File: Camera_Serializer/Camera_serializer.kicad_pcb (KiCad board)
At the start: 4 copper layers, 38.1 x 38.1 mm, 87 parts, among them J2 F32Q-1A7H1-11022, Q1 BSS138, Q2 BSS138, U2 PUSB3FR4Z, U3 TPS62133RGTR, U4 TPS62131RGTT, U5 TPS73601DBVR, U6 MIC5528-3.3YMT-TR

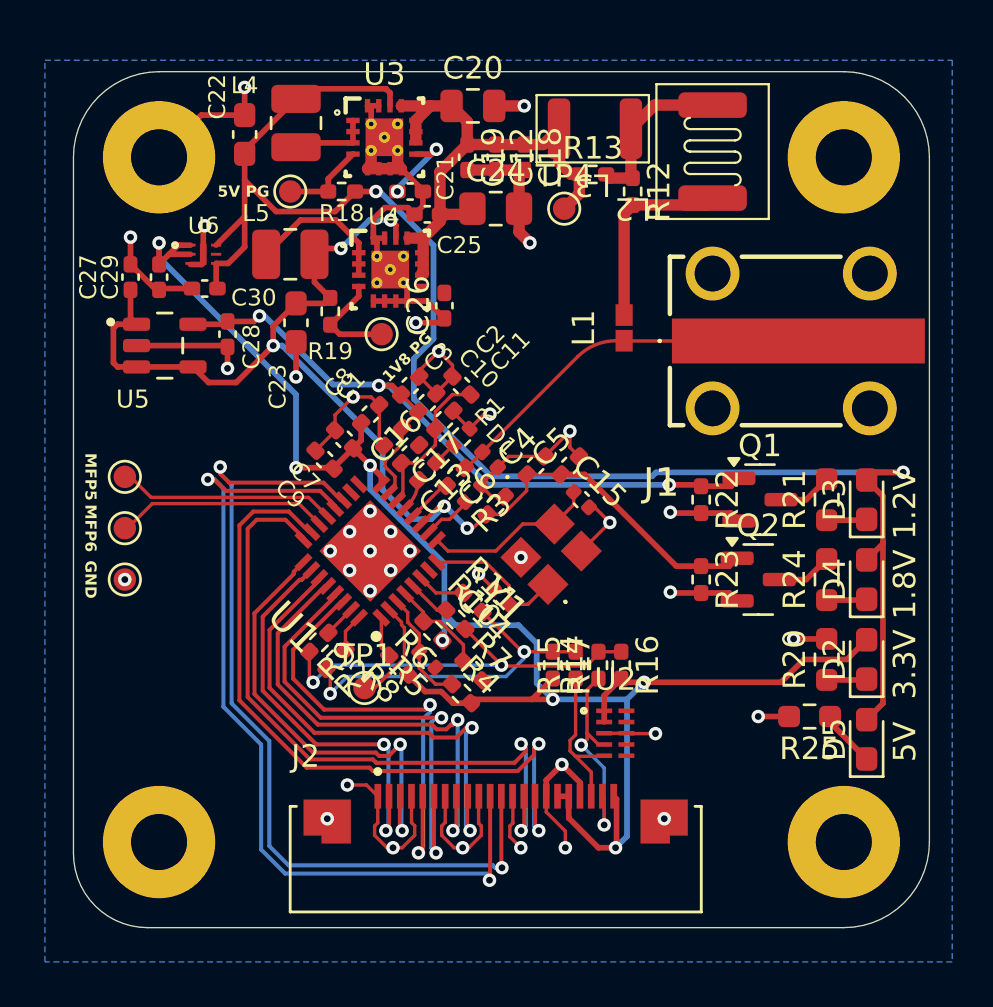
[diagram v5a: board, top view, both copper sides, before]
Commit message: Finished differential routing
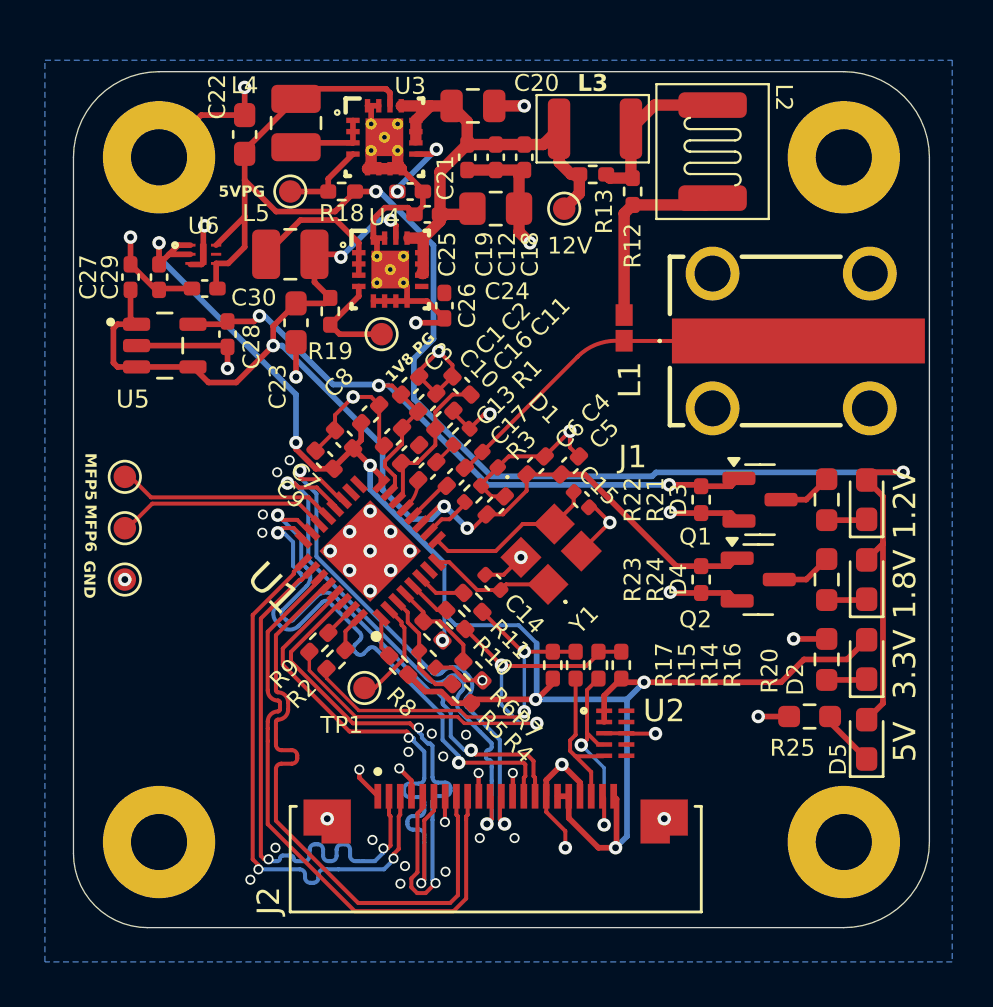
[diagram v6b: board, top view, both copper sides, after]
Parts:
- removed 1V8 PG: TestPoint, TestPoint:TestPoint_Pad_D1.0mm
- removed 5V PG: TestPoint, TestPoint:TestPoint_Pad_D1.0mm
- removed GND, MFP5, MFP6: TestPoint, TestPoint:TestPoint_Pad_D1.0mm
- added TP2: TestPoint, TestPoint:TestPoint_Pad_D1.0mm, F.Cu at (134.4, 94.7)
- added TP3: TestPoint, TestPoint:TestPoint_Pad_D1.0mm, F.Cu at (134.4, 97.0)
- added TP5: TestPoint, TestPoint:TestPoint_Pad_D1.0mm, F.Cu at (141.7, 82.0)
- added TP7: TestPoint, TestPoint:TestPoint_Pad_D1.0mm, F.Cu at (145.8, 88.4)
- added TP8: TestPoint, TestPoint:TestPoint_Pad_D1.0mm, F.Cu at (134.4, 99.3)
- moved C14 0.74 mm to (150.7, 99.4)
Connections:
- C26 pad 2: Net-(U4-SS_TR) -> unconnected-(C26-Pad2)
- L5 pad 1: Net-(L5-Pad1) -> unconnected-(L5-Pad1)
- R19 pad 2: Net-(U4-PG) -> Net-(R19-Pad2)
- U4 pad 1: Net-(L5-Pad1) -> unconnected-(U4-SW-Pad1)
- U4 pad 10: +12V -> unconnected-(U4-AVIN-Pad10)
- U4 pad 11: +12V -> unconnected-(U4-PVIN-Pad11)
- U4 pad 12: +12V -> unconnected-(U4-PVIN-Pad12)
- U4 pad 13: +12V -> unconnected-(U4-EN-Pad13)
- U4 pad 14: +1V8 -> unconnected-(U4-VOS-Pad14)
- U4 pad 15: GND -> unconnected-(U4-PGND-Pad15)
- U4 pad 16: GND -> unconnected-(U4-PGND-Pad16)
- U4 pad 17: GND -> unconnected-(U4-EP-Pad17)
- U4 pad 18: (no net) -> GND
- U4 pad 19: (no net) -> GND
- U4 pad 2: Net-(L5-Pad1) -> unconnected-(U4-SW-Pad2)
- U4 pad 20: (no net) -> GND
- U4 pad 21: (no net) -> GND
- U4 pad 3: Net-(L5-Pad1) -> unconnected-(U4-SW-Pad3)
- U4 pad 4: Net-(U4-PG) -> unconnected-(U4-PG-Pad4)
- U4 pad 5: GND -> unconnected-(U4-FB-Pad5)
- U4 pad 6: GND -> unconnected-(U4-AGND-Pad6)
- U4 pad 7: GND -> unconnected-(U4-FSW-Pad7)
- U4 pad 8: GND -> unconnected-(U4-DEF-Pad8)
- U4 pad 9: Net-(U4-SS_TR) -> unconnected-(U4-SS_TR-Pad9)
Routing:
- net /csi/CSI.D2_N: track 38.5 -> 24.6 mm
- net /csi/CSI.D2_P: track 38.0 -> 24.6 mm
- net /csi/CSI.D3_P: track 32.5 -> 24.6 mm
- net /csi/CSI.CK_N: track 21.0 -> 27.7 mm, vias 2 -> 0
- net Net-(L5-Pad1): track 6.61 -> 0.00 mm
- net (no net): track 0.00 -> 6.61 mm, vias 0 -> 2
- net GND: track 102.3 -> 96.1 mm, vias 38 -> 53
- net /csi/CSI.D0_N: track 18.5 -> 24.6 mm
- net /csi/CSI.D3_N: track 30.4 -> 24.6 mm
- net /csi/I2C.SDA: track 18.1 -> 23.6 mm
- net /csi/CSI.CK_P: track 22.3 -> 27.7 mm, vias 2 -> 0
- net /csi/CSI.D0_P: track 20.1 -> 24.6 mm
- net /csi/CSI.D1_N: track 20.6 -> 24.7 mm
- net /csi/CSI.D1_P: track 21.5 -> 24.6 mm
- net /csi/I2C.SCL: track 15.6 -> 17.6 mm
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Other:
- board text added: "12V"
- board text added: "1V8 PG"
- board text added: "5VPG"
- board text added: "GND"
- board text added: "MFP5"
- board text added: "MFP6"

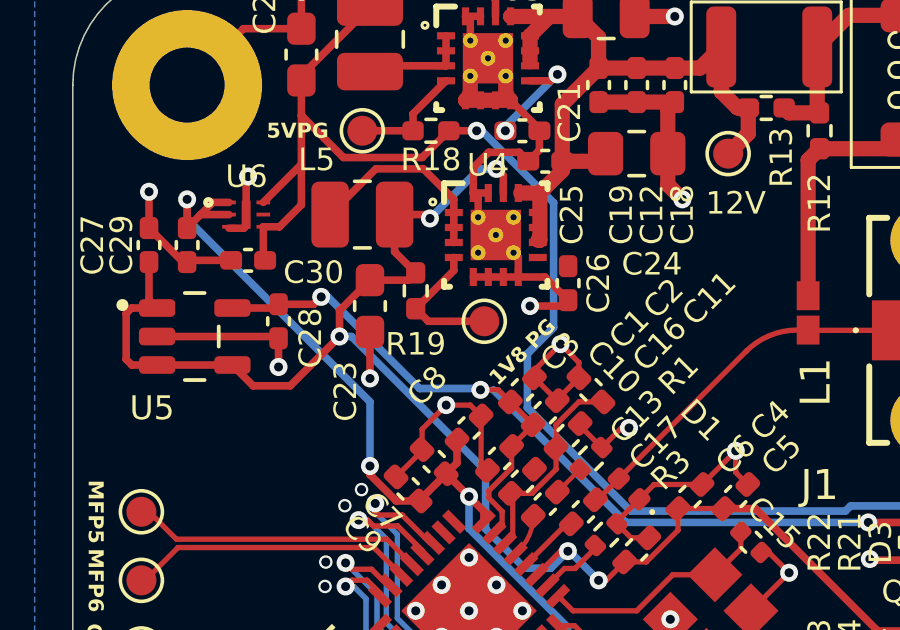
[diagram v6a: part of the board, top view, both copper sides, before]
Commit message: Fixed power IC disconnected on schematic
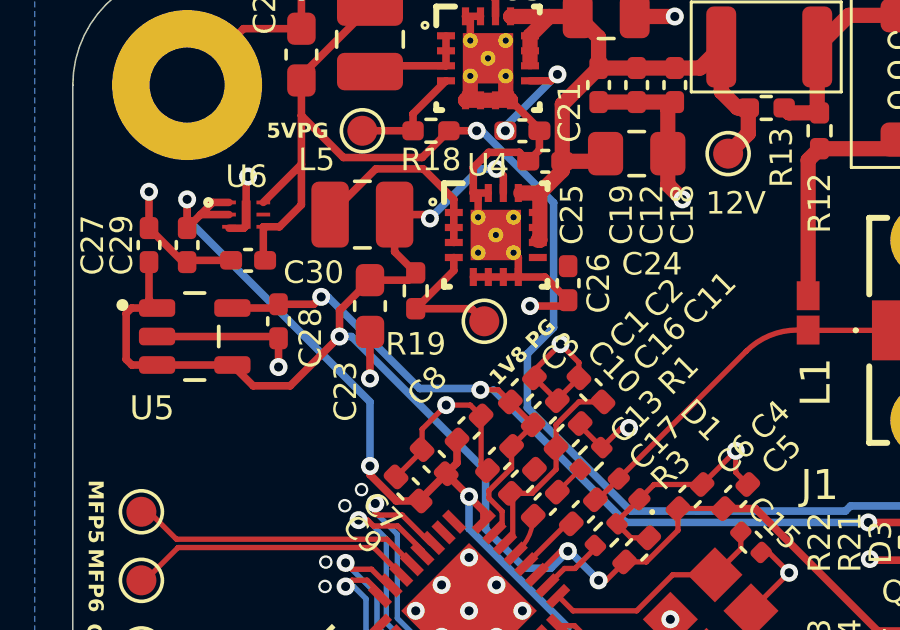
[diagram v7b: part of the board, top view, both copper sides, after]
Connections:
- C26 pad 2: unconnected-(C26-Pad2) -> Net-(U4-SS_TR)
- L5 pad 1: unconnected-(L5-Pad1) -> Net-(L5-Pad1)
- R19 pad 2: Net-(R19-Pad2) -> Net-(U4-PG)
- TP7 pad 1: Net-(R19-Pad2) -> Net-(U4-PG)
- U4 pad 1: unconnected-(U4-SW-Pad1) -> Net-(L5-Pad1)
- U4 pad 10: unconnected-(U4-AVIN-Pad10) -> +12V
- U4 pad 11: unconnected-(U4-PVIN-Pad11) -> +12V
- U4 pad 12: unconnected-(U4-PVIN-Pad12) -> +12V
- U4 pad 13: unconnected-(U4-EN-Pad13) -> +12V
- U4 pad 14: unconnected-(U4-VOS-Pad14) -> +1V8
- U4 pad 15: unconnected-(U4-PGND-Pad15) -> GND
- U4 pad 16: unconnected-(U4-PGND-Pad16) -> GND
- U4 pad 17: unconnected-(U4-EP-Pad17) -> GND
- U4 pad 2: unconnected-(U4-SW-Pad2) -> Net-(L5-Pad1)
- U4 pad 3: unconnected-(U4-SW-Pad3) -> Net-(L5-Pad1)
- U4 pad 4: unconnected-(U4-PG-Pad4) -> Net-(U4-PG)
- U4 pad 5: unconnected-(U4-FB-Pad5) -> GND
- U4 pad 6: unconnected-(U4-AGND-Pad6) -> GND
- U4 pad 7: unconnected-(U4-FSW-Pad7) -> GND
- U4 pad 8: unconnected-(U4-DEF-Pad8) -> GND
- U4 pad 9: unconnected-(U4-SS_TR-Pad9) -> Net-(U4-SS_TR)
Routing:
- net Net-(L5-Pad1): track 0.00 -> 6.61 mm
- net (no net): track 6.61 -> 0.00 mm
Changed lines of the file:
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@@
 	(net 10 "Net-(U3-SS_TR)")
 	(net 11 "+5V")
-	(net 12 "unconnected-(C26-Pad2)")
+	(net 12 "Net-(U4-SS_TR)")
 	(net 13 "/GMSL_Connector/SIOP_COAX")
 	(net 14 "Net-(D2-K)")
@@
 	(net 28 "/csi/CSI.CK_N")
 	(net 29 "Net-(L4-Pad1)")
-	(net 30 "unconnected-(L5-Pad1)")
+	(net 30 "Net-(L5-Pad1)")
 	(net 31 "Net-(Q1-D)")
 	(net 32 "Net-(Q2-D)")
@@
 	(net 55 "Net-(L2-Pad2)")
 	(net 56 "Net-(D5-K)")
-	(net 57 "Net-(R19-Pad2)")
-	(net 58 "unconnected-(U4-SS_TR-Pad9)")
-	(net 59 "unconnected-(U4-SW-Pad3)")
-	(net 60 "unconnected-(U4-SW-Pad1)")
-	(net 61 "unconnected-(U4-FB-Pad5)")
-	(net 62 "unconnected-(U4-EN-Pad13)")
-	(net 63 "unconnected-(U4-PGND-Pad15)")
-	(net 64 "unconnected-(U4-VOS-Pad14)")
-	(net 65 "unconnected-(U4-PVIN-Pad11)")
-	(net 66 "unconnected-(U4-AVIN-Pad10)")
-	(net 67 "unconnected-(U4-FSW-Pad7)")
-	(net 68 "unconnected-(U4-EP-Pad17)")
-	(net 69 "unconnected-(U4-SW-Pad2)")
-	(net 70 "unconnected-(U4-DEF-Pad8)")
-	(net 71 "unconnected-(U4-PVIN-Pad12)")
-	(net 72 "unconnected-(U4-PGND-Pad16)")
-	(net 73 "unconnected-(U4-AGND-Pad6)")
-	(net 74 "unconnected-(U4-PG-Pad4)")
 	(footprint "Diode_SMD:D_0402_1005Metric"
 		(layer "F.Cu")
@@
 			(layers "F.Cu" "F.Paste" "F.Mask")
 			(roundrect_rratio 0.2)
-			(net 30 "unconnected-(L5-Pad1)")
+			(net 30 "Net-(L5-Pad1)")
 			(pinfunction "1")
 			(pintype "passive")
@@
 			(size 0.24 0.599999)
 			(layers "F.Cu" "F.Paste" "F.Mask")
-			(net 60 "unconnected-(U4-SW-Pad1)")
+			(net 30 "Net-(L5-Pad1)")
 			(pinfunction "SW")
 			(pintype "power_in")
@@
 			(size 0.24 0.599999)
 			(layers "F.Cu" "F.Paste" "F.Mask")
-			(net 69 "unconnected-(U4-SW-Pad2)")
+			(net 30 "Net-(L5-Pad1)")
 			(pinfunction "SW")
 			(pintype "power_in")
@@
 			(size 0.24 0.599999)
 			(layers "F.Cu" "F.Paste" "F.Mask")
-			(net 59 "unconnected-(U4-SW-Pad3)")
+			(net 30 "Net-(L5-Pad1)")
 			(pinfunction "SW")
 			(pintype "power_in")
@@
 			(size 0.24 0.599999)
 			(layers "F.Cu" "F.Paste" "F.Mask")
-			(net 74 "unconnected-(U4-PG-Pad4)")
+			(net 39 "Net-(U4-PG)")
 			(pinfunction "PG")
 			(pintype "open_collector")
@@
 			(size 0.24 0.599999)
 			(layers "F.Cu" "F.Paste" "F.Mask")
-			(net 61 "unconnected-(U4-FB-Pad5)")
+			(net 7 "GND")
 			(pinfunction "FB")
 			(pintype "input")
@@
 			(size 0.24 0.599999)
 			(layers "F.Cu" "F.Paste" "F.Mask")
-			(net 73 "unconnected-(U4-AGND-Pad6)")
+			(net 7 "GND")
 			(pinfunction "AGND")
 			(pintype "power_in")
@@
 			(size 0.24 0.599999)
 			(layers "F.Cu" "F.Paste" "F.Mask")
-			(net 67 "unconnected-(U4-FSW-Pad7)")
+			(net 7 "GND")
 			(pinfunction "FSW")
 			(pintype "input")
@@
 			(size 0.24 0.599999)
 			(layers "F.Cu" "F.Paste" "F.Mask")
-			(net 70 "unconnected-(U4-DEF-Pad8)")
+			(net 7 "GND")
 			(pinfunction "DEF")
 			(pintype "input")
@@
 			(size 0.24 0.599999)
 			(layers "F.Cu" "F.Paste" "F.Mask")
-			(net 58 "unconnected-(U4-SS_TR-Pad9)")
+			(net 12 "Net-(U4-SS_TR)")
 			(pinfunction "SS_TR")
 			(pintype "input")
@@
 			(size 0.24 0.599999)
 			(layers "F.Cu" "F.Paste" "F.Mask")
-			(net 66 "unconnected-(U4-AVIN-Pad10)")
+			(net 9 "+12V")
 			(pinfunction "AVIN")
 			(pintype "power_in")
@@
 			(size 0.24 0.599999)
 			(layers "F.Cu" "F.Paste" "F.Mask")
-			(net 65 "unconnected-(U4-PVIN-Pad11)")
+			(net 9 "+12V")
 			(pinfunction "PVIN")
 			(pintype "power_in")
@@
 			(size 0.24 0.599999)
 			(layers "F.Cu" "F.Paste" "F.Mask")
-			(net 71 "unconnected-(U4-PVIN-Pad12)")
+			(net 9 "+12V")
 			(pinfunction "PVIN")
 			(pintype "power_in")
@@
 			(size 0.24 0.599999)
 			(layers "F.Cu" "F.Paste" "F.Mask")
-			(net 62 "unconnected-(U4-EN-Pad13)")
+			(net 9 "+12V")
 			(pinfunction "EN")
 			(pintype "input")
@@
 			(size 0.24 0.599999)
 			(layers "F.Cu" "F.Paste" "F.Mask")
-			(net 64 "unconnected-(U4-VOS-Pad14)")
+			(net 2 "+1V8")
 			(pinfunction "VOS")
 			(pintype "input")
@@
 			(size 0.24 0.599999)
 			(layers "F.Cu" "F.Paste" "F.Mask")
-			(net 63 "unconnected-(U4-PGND-Pad15)")
+			(net 7 "GND")
 			(pinfunction "PGND")
 			(pintype "power_in")
@@
 			(size 0.24 0.599999)
 			(layers "F.Cu" "F.Paste" "F.Mask")
-			(net 72 "unconnected-(U4-PGND-Pad16)")
+			(net 7 "GND")
 			(pinfunction "PGND")
 			(pintype "power_in")
@@
 			(size 1.679999 1.679999)
 			(layers "F.Cu" "F.Mask")
-			(net 68 "unconnected-(U4-EP-Pad17)")
+			(net 7 "GND")
 			(pinfunction "EP")
 			(pintype "power_in")
@@
 			(layers "F.Cu" "F.Paste" "F.Mask")
 			(roundrect_rratio 0.25)
-			(net 57 "Net-(R19-Pad2)")
+			(net 39 "Net-(U4-PG)")
 			(pintype "passive")
 		)
@@
 			(size 1 1)
 			(layers "F.Cu" "F.Mask")
-			(net 57 "Net-(R19-Pad2)")
+			(net 39 "Net-(U4-PG)")
 			(pinfunction "1")
 			(pintype "passive")
@@
 			(layers "F.Cu" "F.Paste" "F.Mask")
 			(roundrect_rratio 0.25)
-			(net 12 "unconnected-(C26-Pad2)")
+			(net 12 "Net-(U4-SS_TR)")
 			(pintype "passive")
 		)
@@
 			(extension_offset 0.5) keep_text_aligned)
 	)
-	(segment
-		(start 143.764 83.312)
-		(end 144.78 84.328)
-		(width 0.254)
-		(layer "F.Cu")
-		(net 0)
-	)
-	(segment
-		(start 140.657 84.836)
-		(end 142.181 83.312)
-		(width 0.254)
-		(layer "F.Cu")
-		(net 0)
-	)
-	(segment
-		(start 144.78 84.328)
-		(end 144.78 85.766001)
-		(width 0.254)
-		(layer "F.Cu")
-		(net 0)
-	)
-	(segment
-		(start 142.181 83.312)
-		(end 143.764 83.312)
-		(width 0.254)
-		(layer "F.Cu")
-		(net 0)
-	)
 	(via
 		(at 141.1478 94.5388)
@@
 	)
 	(segment
+		(start 143.764 83.312)
+		(end 144.78 84.328)
+		(width 0.254)
+		(layer "F.Cu")
+		(net 30)
+	)
+	(segment
+		(start 140.657 84.836)
+		(end 142.181 83.312)
+		(width 0.254)
+		(layer "F.Cu")
+		(net 30)
+	)
+	(segment
+		(start 144.78 84.328)
+		(end 144.78 85.766001)
+		(width 0.254)
+		(layer "F.Cu")
+		(net 30)
+	)
+	(segment
+		(start 142.181 83.312)
+		(end 143.764 83.312)
+		(width 0.254)
+		(layer "F.Cu")
+		(net 30)
+	)
+	(segment
 		(start 163.576 95.758)
 		(end 164.6955 95.758)
@@
 	)
 	(segment
-		(start 143.9285 88.392)
-		(end 143.51 87.9735)
+		(start 145.3775 87.9735)
+		(end 145.796 88.392)
 		(width 0.254)
 		(layer "F.Cu")
@@
 	)
 	(segment
-		(start 144.78 86.266)
-		(end 144.78 86.7035)
+		(start 144.78 86.7035)
+		(end 143.51 87.9735)
 		(width 0.254)
 		(layer "F.Cu")
@@
 	)
 	(segment
-		(start 143.9285 88.392)
-		(end 145.796 88.392)
+		(start 144.78 86.266)
+		(end 144.78 86.7035)
 		(width 0.254)
 		(layer "F.Cu")
@@
 	)
 	(segment
-		(start 144.78 86.7035)
-		(end 143.51 87.9735)
+		(start 143.51 87.9735)
+		(end 145.3775 87.9735)
 		(width 0.254)
 		(layer "F.Cu")

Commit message: Finished Rev1
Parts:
- added REF**: tuna_front_copper, KicadLibraries:tuna_front_copper, B.Cu at (135.1, 96.0)
- moved TP2 1.08 mm to (135.1, 94.0)
- moved TP8 0.94 mm to (135.2, 98.8)
- moved TP3 0.92 mm to (135.1, 96.5)
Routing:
- net GND: track 96.1 -> 99.3 mm, vias 53 -> 66
- net Net-(U4-SS_TR): track 0.00 -> 1.13 mm
- net Net-(U1-MFP6): track 9.49 -> 8.52 mm
- net (no net): vias 2 -> 0
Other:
- board text added: "Camera Serializer Rev1 Mars Rover Design Team Missouri S&T, 2025 Jesse Deuel"
